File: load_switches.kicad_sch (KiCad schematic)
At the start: 15 parts, among them U10 SY6283ADRC, U11 SY6283ADRC, U15 SY6283ADRC, U9 SY6283ADRC

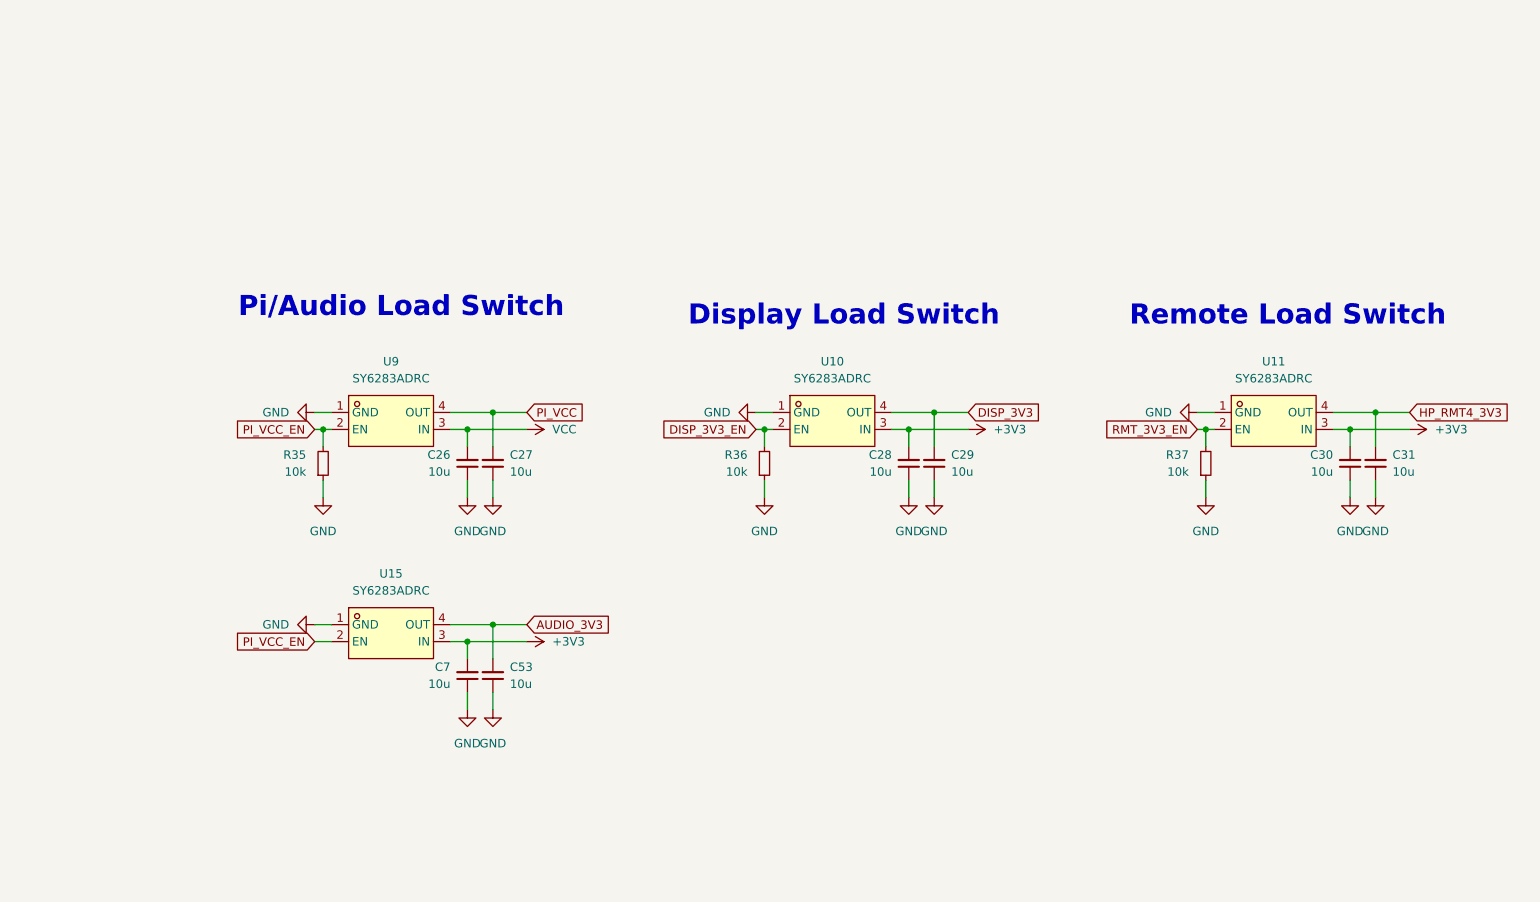
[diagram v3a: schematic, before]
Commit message: schem: migrate away from LCSC exclusive parts
- layout: migrate away from lcsc footprints
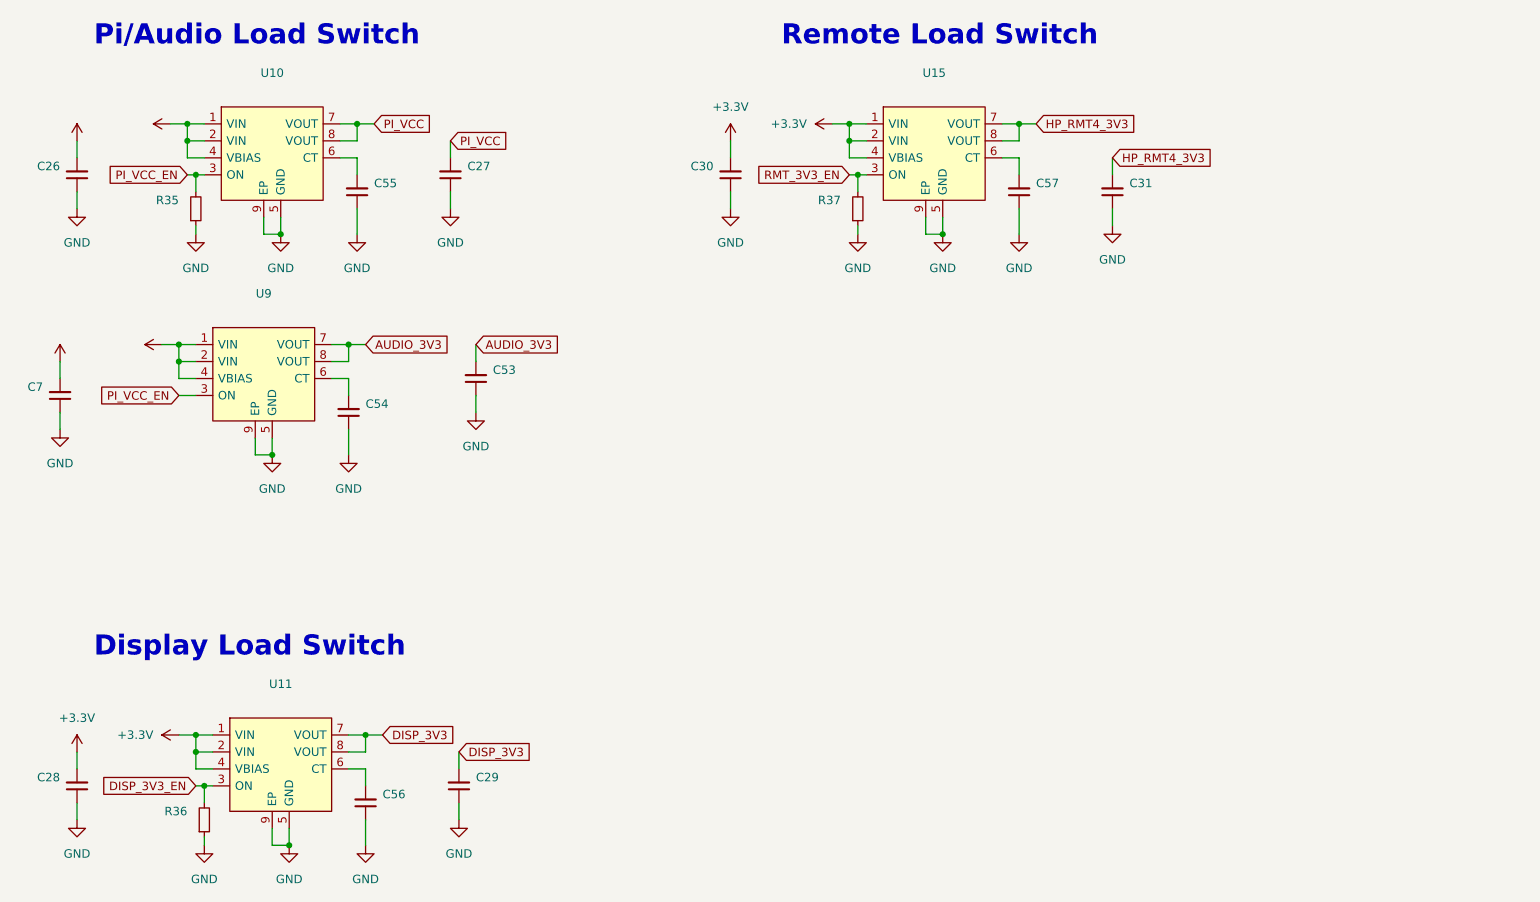
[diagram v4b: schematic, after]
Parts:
- removed U10, U11, U15, U9: SY6283ADRC, lcsc:DFN-4_L1.6-W1.2-P0.50-BL, symbol lcsc:SY6283ADRC
- added C54, C55, C56, C57: (no value), symbol Device:C_Small
- added U10, U11, U15, U9: (no value), symbol gigahawk:TPS22965TDSGRQ1
- C26, C27, C28, C29, C30, C31, C53, C7: value 10u -> (none); footprint Capacitor_SMD:C_0402_1005Metric -> (none)
- R35, R36, R37: value 10k -> (none); footprint Resistor_SMD:R_0402_1005Metric -> (none)
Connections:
- net +3V3: now also U11.1 (VIN), U11.2 (VIN), U11.4 (VBIAS), U15.1 (VIN), U15.2 (VIN), U15.4 (VBIAS), U9.1 (VIN), U9.2 (VIN), U9.4 (VBIAS)
- net AUDIO_3V3: now also U9.7 (VOUT), U9.8 (VOUT)
- net DISP_3V3: now also U11.7 (VOUT), U11.8 (VOUT)
- net DISP_3V3_EN: now also U11.3 (ON)
- net GND: now also C54.1, C55.1, C56.1, C57.1, U10.5 (GND), U10.9 (EP), U11.5 (GND), U11.9 (EP), U15.5 (GND), U15.9 (EP), U9.5 (GND), U9.9 (EP)
- net HP_RMT4_3V3: now also U15.7 (VOUT), U15.8 (VOUT)
- net PI_VCC: now also U10.7 (VOUT), U10.8 (VOUT)
- net PI_VCC_EN: now also U10.3 (ON), U9.3 (ON)
- net RMT_3V3_EN: now also U15.3 (ON)
- net VCC: now also U10.1 (VIN), U10.2 (VIN), U10.4 (VBIAS)
- new net: C55.2, U10.6 (CT)
- new net: C56.2, U11.6 (CT)
- new net: C54.2, U9.6 (CT)
- new net: C57.2, U15.6 (CT)
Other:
- moved on the sheet: C26, C27, C28, C29, C30, C31, C53, C7, R35, R36, R37

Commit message: layout: update footprint for TP4056M
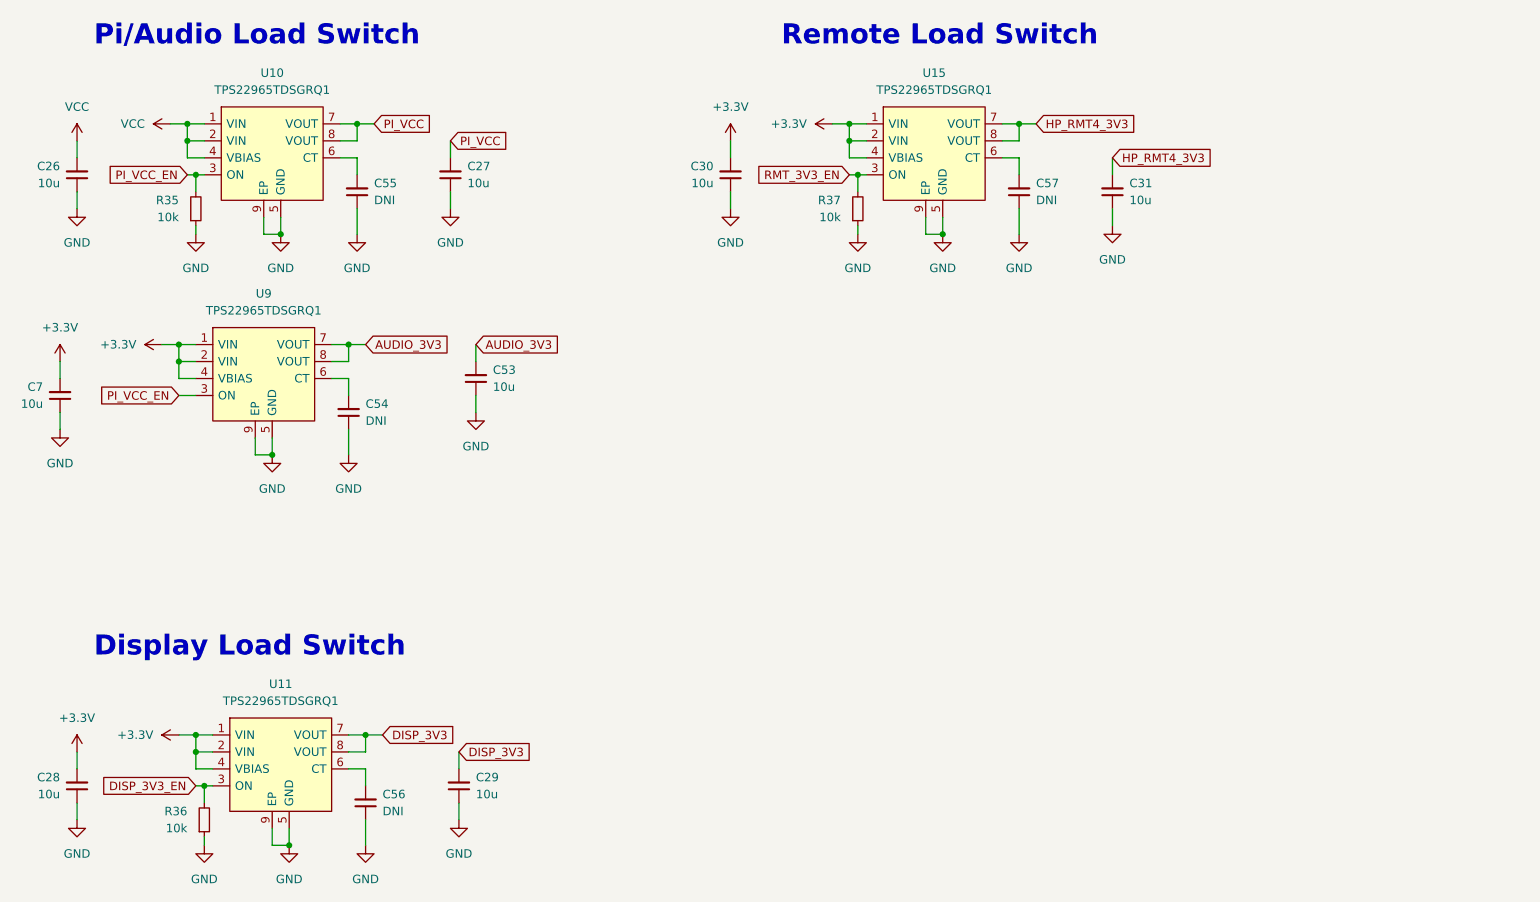
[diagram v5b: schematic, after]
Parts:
- C26, C27, C28, C29, C30, C31, C53, C7: value (none) -> 10u; footprint (none) -> Capacitor_SMD:C_0402_1005Metric
- C54, C55, C56, C57: value (none) -> DNI; footprint (none) -> Capacitor_SMD:C_0402_1005Metric
- R35, R36, R37: value (none) -> 10k; footprint (none) -> Resistor_SMD:R_0402_1005Metric
- U10, U11, U15, U9: value (none) -> TPS22965TDSGRQ1; footprint (none) -> Package_SON:WSON-8-1EP_2x2mm_P0.5mm_EP0.9x1.6mm

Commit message: layout: preliminary layout of most of board
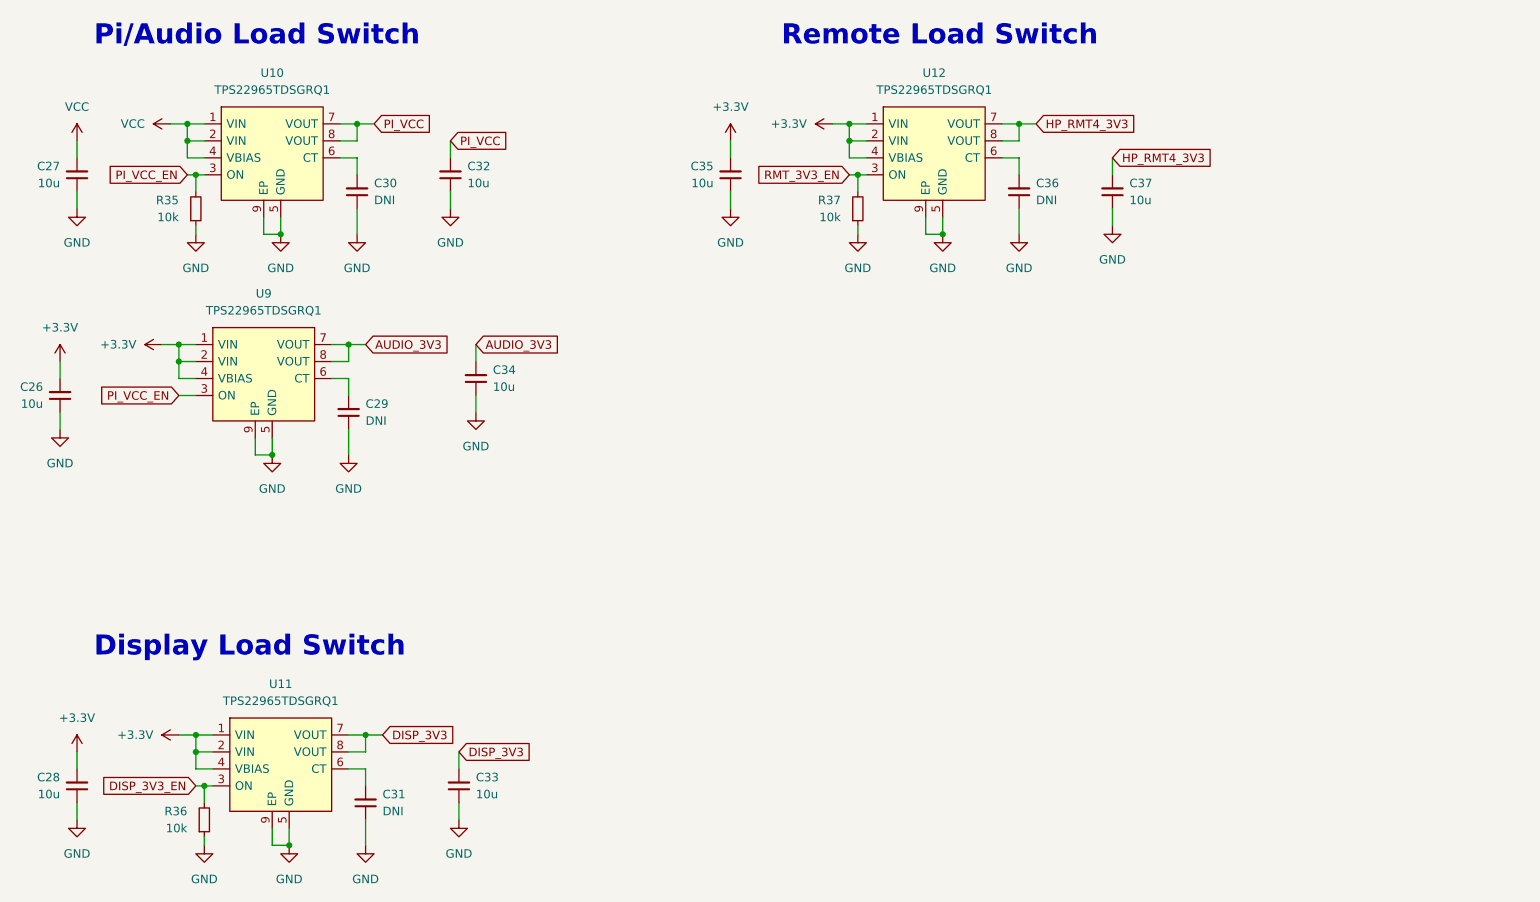
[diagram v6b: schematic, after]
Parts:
- renumbered C7 to C26, C26 to C27, C54 to C29, C55 to C30, C56 to C31, C27 to C32, C29 to C33, C53 to C34, C30 to C35, C57 to C36, C31 to C37, U15 to U12

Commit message: layout, routing: relayout and reroute board
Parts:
- C26, C27, C28, C32, C33, C34, C35, C37: value 10u -> (none); footprint Capacitor_SMD:C_0402_1005Metric -> (none)
- C29, C30, C31, C36: value DNI -> (none); footprint Capacitor_SMD:C_0402_1005Metric -> (none)
- R35, R36, R37: value 10k -> (none); footprint Resistor_SMD:R_0402_1005Metric -> (none)
- U10, U11, U12, U9: value TPS22965TDSGRQ1 -> (none); footprint Package_SON:WSON-8-1EP_2x2mm_P0.5mm_EP0.9x1.6mm -> (none)
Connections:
- net PI_SW_CT: now reaches C30.2, U10.6 (CT)
- net DISP_SW_CT: now reaches C31.2, U11.6 (CT)
- net AUDIO_SW_CT: now reaches C29.2, U9.6 (CT)
- net RMT_SW_CT: now reaches C36.2, U12.6 (CT)
